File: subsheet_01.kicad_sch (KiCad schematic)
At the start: 0 parts

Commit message: Updated kicad-symbol-generated
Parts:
- added A1: FTDI_232H_MODULE_USB-C_VERSION_PHY, symbol 2264_bob_ft232h_usbc:FTDI_232H_MODULE_USB-C_VERSION_PHY
- added A2: FTDI_232H_MODULE_USB-A_VERSION_PHY, symbol bob_ft232h_usba:FTDI_232H_MODULE_USB-A_VERSION_PHY
- added J1: JTAG, symbol Connector_Generic:Conn_02x04_Odd_Even
- added J2: VPP connector, symbol Connector_Generic:Conn_02x01
- added J3: DC-DC converter, symbol Connector_Generic:Conn_01x04
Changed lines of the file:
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@@
     (company "Sporniket.com")
   )
+  (symbol (lib_id "Connector_Generic:Conn_01x04") (at 138.43 149.86 0) (unit 1)
+    (in_bom yes) (on_board yes) (dnp no)
+    (property "Reference" "J3" (at 138.43 144.78 0)
+      (effects (font (size 1.27 1.27)))
+    )
+    (property "Value" "DC-DC converter" (at 138.43 157.48 0)
+      (effects (font (size 1.27 1.27)))
+    )
+    (property "Footprint" "" (at 138.43 149.86 0)
+      (effects (font (size 1.27 1.27)) hide)
+    )
+    (property "Datasheet" "~" (at 138.43 149.86 0)
+      (effects (font (size 1.27 1.27)) hide)
+    )
+    (pin "4")
+    (pin "3")
+    (pin "2")
+    (pin "1")
+    (instances
+      (project "thomson-mo5--gate-array-development-board"
+        (path "/ba04bd6b-eda4-4852-8472-8c9205b270a0/aa83933c-d278-4584-ab2e-5bb5678ba36b"
+          (reference "J3") (unit 1)
+        )
+      )
+    )
+  )
+  (symbol (lib_id "bob_ft232h_usba:FTDI_232H_MODULE_USB-A_VERSION_PHY") (at 101.6 74.93 0) (unit 1)
+    (in_bom yes) (on_board yes) (dnp no)
+    (property "Reference" "A2" (at 93.98 55.88 0)
+      (effects (font (size 1.27 1.27)) (justify left top))
+    )
+    (property "Value" "FTDI_232H_MODULE_USB-A_VERSION_PHY" (at 93.98 58.42 0)
+      (effects (font (size 1.27 1.27) bold) (justify left top))
+    )
+    (property "Footprint" "" (at 101.6 74.93 0)
+      (effects (font (size 1.27 1.27)) hide)
+    )
+    (property "Datasheet" "_None_" (at 93.98 50.8 0)
+      (effects (font (size 1.27 1.27)) (justify left top) hide)
+    )
+    (pin "3")
+    (pin "2")
+    (pin "20")
+    (pin "19")
+    (pin "16")
+    (pin "13")
+    (pin "11")
+    (pin "7")
+    (pin "17")
+    (pin "1")
+    (pin "15")
+    (pin "5")
+    (pin "9")
+    (pin "4")
+    (pin "6")
+    (pin "8")
+    (pin "10")
+    (pin "14")
+    (pin "12")
+    (pin "18")
+    (instances
+      (project "thomson-mo5--gate-array-development-board"
+        (path "/ba04bd6b-eda4-4852-8472-8c9205b270a0/aa83933c-d278-4584-ab2e-5bb5678ba36b"
+          (reference "A2") (unit 1)
+        )
+      )
+    )
+  )
+  (symbol (lib_id "Connector_Generic:Conn_02x04_Odd_Even") (at 99.06 124.46 0) (unit 1)
+    (in_bom yes) (on_board yes) (dnp no)
+    (property "Reference" "J1" (at 100.33 119.38 0)
+      (effects (font (size 1.27 1.27)))
+    )
+    (property "Value" "JTAG" (at 100.33 132.08 0)
+      (effects (font (size 1.27 1.27)))
+    )
+    (property "Footprint" "" (at 99.06 124.46 0)
+      (effects (font (size 1.27 1.27)) hide)
+    )
+    (property "Datasheet" "~" (at 99.06 124.46 0)
+      (effects (font (size 1.27 1.27)) hide)
+    )
+    (pin "1")
+    (pin "4")
+    (pin "3")
+    (pin "2")
+    (pin "6")
+    (pin "7")
+    (pin "5")
+    (pin "8")
+    (instances
+      (project "thomson-mo5--gate-array-development-board"
+        (path "/ba04bd6b-eda4-4852-8472-8c9205b270a0/aa83933c-d278-4584-ab2e-5bb5678ba36b"
+          (reference "J1") (unit 1)
+        )
+      )
+    )
+  )
+  (symbol (lib_id "Connector_Generic:Conn_02x01") (at 99.06 147.32 0) (unit 1)
+    (in_bom yes) (on_board yes) (dnp no)
+    (property "Reference" "J2" (at 100.33 144.78 0)
+      (effects (font (size 1.27 1.27)))
+    )
+    (property "Value" "VPP connector" (at 100.33 149.86 0)
+      (effects (font (size 1.27 1.27)))
+    )
+    (property "Footprint" "" (at 99.06 147.32 0)
+      (effects (font (size 1.27 1.27)) hide)
+    )
+    (property "Datasheet" "~" (at 99.06 147.32 0)
+      (effects (font (size 1.27 1.27)) hide)
+    )
+    (pin "2")
+    (pin "1")
+    (instances
+      (project "thomson-mo5--gate-array-development-board"
+        (path "/ba04bd6b-eda4-4852-8472-8c9205b270a0/aa83933c-d278-4584-ab2e-5bb5678ba36b"
+          (reference "J2") (unit 1)
+        )
+      )
+    )
+  )
+  (symbol (lib_id "2264_bob_ft232h_usbc:FTDI_232H_MODULE_USB-C_VERSION_PHY") (at 101.6 38.1 0) (unit 1)
+    (in_bom yes) (on_board yes) (dnp no)
+    (property "Reference" "A1" (at 92.71 17.78 0)
+      (effects (font (size 1.27 1.27)) (justify left top))
+    )
+    (property "Value" "FTDI_232H_MODULE_USB-C_VERSION_PHY" (at 92.71 20.32 0)
+      (effects (font (size 1.27 1.27) bold) (justify left top))
+    )
+    (property "Footprint" "" (at 101.6 38.1 0)
+      (effects (font (size 1.27 1.27)) hide)
+    )
+    (property "Datasheet" "https://learn.adafruit.com/adafruit-ft232h-breakout/wiring" (at 92.71 12.7 0)
+      (effects (font (size 1.27 1.27)) (justify left top) hide)
+    )
+    (pin "9")
+    (pin "6")
+    (pin "14")
+    (pin "5")
+    (pin "20")
+    (pin "2")
+    (pin "18")
+    (pin "12")
+    (pin "11")
+    (pin "10")
+    (pin "1")
+    (pin "4")
+    (pin "22")
+    (pin "16")
+    (pin "21")
+    (pin "3")
+    (pin "7")
+    (pin "15")
+    (pin "17")
+    (pin "8")
+    (pin "13")
+    (pin "19")
+    (instances
+      (project "thomson-mo5--gate-array-development-board"
+        (path "/ba04bd6b-eda4-4852-8472-8c9205b270a0/aa83933c-d278-4584-ab2e-5bb5678ba36b"
+          (reference "A1") (unit 1)
+        )
+      )
+    )
+  )
 )

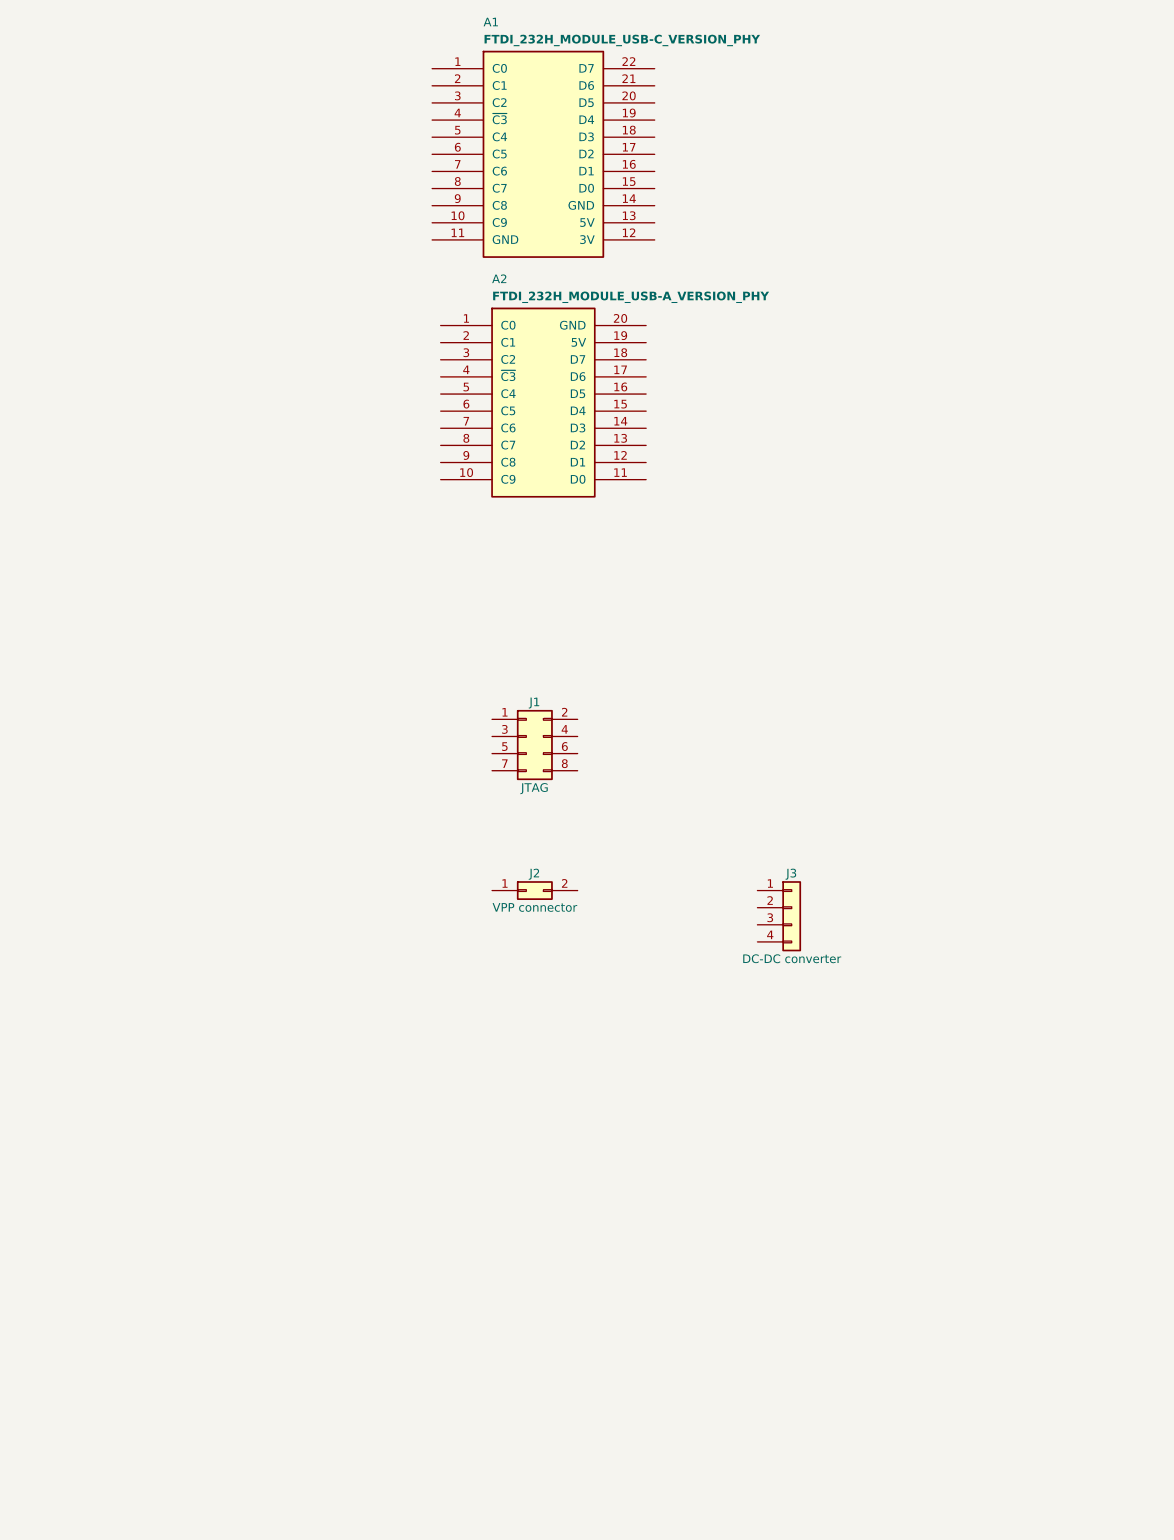
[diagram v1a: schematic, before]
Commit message: done schematics : ftdi module, JTAG, DC converters modules
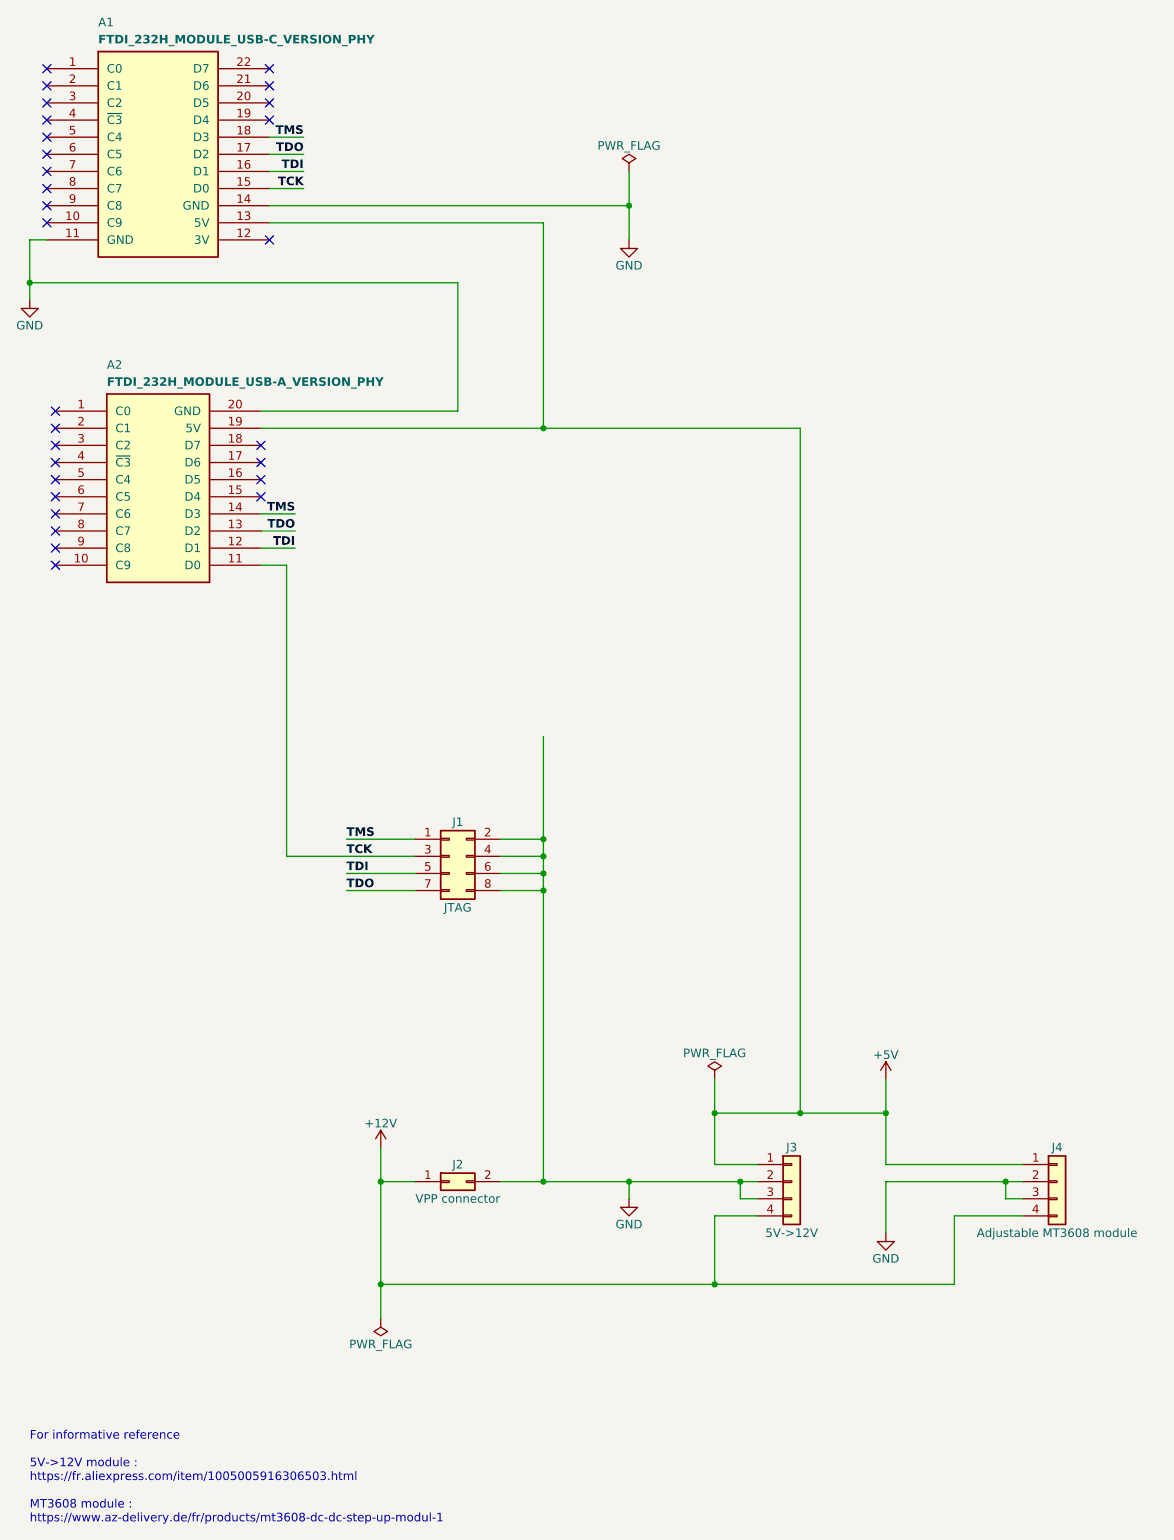
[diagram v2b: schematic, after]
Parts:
- added J4: Adjustable MT3608 module, symbol Connector_Generic:Conn_01x04
- J3: value DC-DC converter -> 5V->12V
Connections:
- net +5V: now reaches J3.1 (Pin_1)
- net +5V: now also A1.13 (5V), A2.19 (5V), J4.1 (Pin_1)
- net GND: now reaches J3.2 (Pin_2)
- net GND: now also A1.11 (GND), A1.14 (GND), A2.20 (GND), J1.2 (Pin_2), J1.4 (Pin_4), J1.6 (Pin_6), J1.8 (Pin_8), J2.2 (Pin_2), J3.3 (Pin_3), J4.2 (Pin_2), J4.3 (Pin_3)
- net +12V: now reaches J3.4 (Pin_4)
- net +12V: now also J2.1 (Pin_1), J4.4 (Pin_4)
- net TCK: now reaches A2.11 (D0)
- net TCK: now also A1.15 (D0), J1.3 (Pin_3)
- net TDI: now reaches A2.12 (D1)
- net TDI: now also A1.16 (D1), J1.5 (Pin_5)
- net TDO: now reaches A2.13 (D2)
- net TDO: now also A1.17 (D2), J1.7 (Pin_7)
- net TMS: now reaches A2.14 (D3)
- net TMS: now also A1.18 (D3), J1.1 (Pin_1)
- no-connect marks 0 -> 29
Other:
- note added: "For informative reference 5V->12V module : https://fr.aliexpress.com/item/1005005916306503.html MT3608 module : https://www.az-delivery.de/fr/products/mt3608-dc-dc-step-up-modul-1"
- moved on the sheet: A1, A2, J1, J2, J3

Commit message: done schematics
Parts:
- added D1, D2: LED, symbol Device:LED
- added R1, R2: 3K, symbol Device:R_Small_US
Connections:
- net +12V: now also D2.2 (A)
- net +5V: now also D1.2 (A)
- net GND: now also R1.2, R2.2
- new net: D1.1 (K), R1.1
- new net: D2.1 (K), R2.1

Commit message: assigned footprints, except for ftdi232h breakout boards
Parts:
- D1, D2: footprint (none) -> LED_THT:LED_D3.0mm
- J1: footprint (none) -> Connector_PinHeader_2.54mm:PinHeader_2x04_P2.54mm_Vertical
- J2: footprint (none) -> Connector_PinHeader_2.54mm:PinHeader_2x01_P2.54mm_Vertical
- J3: footprint (none) -> assemblies_power_modules:module_dc_dc_step_up_12V_W10.16mm_H20.5mm_PinSocket_1x04_P2.54mm_Horizontal
- J4: footprint (none) -> assemblies_power_modules:module_mt3608_ajustable_output
- R1, R2: footprint (none) -> commons-passives_THT:Passive_THT_resistor_W2.54mm_L12.70mm
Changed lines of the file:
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@@
       (effects (font (size 1.27 1.27)))
     )
-    (property "Footprint" "" (at 138.43 190.5 0)
+    (property "Footprint" "assemblies_power_modules:module_dc_dc_step_up_12V_W10.16mm_H20.5mm_PinSocket_1x04_P2.54mm_Horizontal" (at 138.43 190.5 0)
       (effects (font (size 1.27 1.27)) hide)
     )
@@
       (effects (font (size 1.27 1.27)) (justify left))
     )
-    (property "Footprint" "" (at 157.48 83.82 0)
+    (property "Footprint" "commons-passives_THT:Passive_THT_resistor_W2.54mm_L12.70mm" (at 157.48 83.82 0)
       (effects (font (size 1.27 1.27)) hide)
     )
@@
       (effects (font (size 1.27 1.27)) (justify left))
     )
-    (property "Footprint" "" (at 161.29 220.98 0)
+    (property "Footprint" "commons-passives_THT:Passive_THT_resistor_W2.54mm_L12.70mm" (at 161.29 220.98 0)
       (effects (font (size 1.27 1.27)) hide)
     )
@@
       (effects (font (size 1.27 1.27)))
     )
-    (property "Footprint" "" (at 152.4 215.9 0)
+    (property "Footprint" "LED_THT:LED_D3.0mm" (at 152.4 215.9 0)
       (effects (font (size 1.27 1.27)) hide)
     )
@@
       (effects (font (size 1.27 1.27)))
     )
-    (property "Footprint" "" (at 148.59 78.74 0)
+    (property "Footprint" "LED_THT:LED_D3.0mm" (at 148.59 78.74 0)
       (effects (font (size 1.27 1.27)) hide)
     )
@@
       (effects (font (size 1.27 1.27)))
     )
-    (property "Footprint" "" (at 87.63 142.24 0)
+    (property "Footprint" "Connector_PinHeader_2.54mm:PinHeader_2x04_P2.54mm_Vertical" (at 87.63 142.24 0)
       (effects (font (size 1.27 1.27)) hide)
     )
@@
       (effects (font (size 1.27 1.27)))
     )
-    (property "Footprint" "" (at 87.63 190.5 0)
+    (property "Footprint" "Connector_PinHeader_2.54mm:PinHeader_2x01_P2.54mm_Vertical" (at 87.63 190.5 0)
       (effects (font (size 1.27 1.27)) hide)
     )
@@
       (effects (font (size 1.27 1.27)))
     )
-    (property "Footprint" "" (at 177.8 190.5 0)
-      (effects (font (size 1.27 1.27)) hide)
-    )
+    (property "Footprint" "assemblies_power_modules:module_mt3608_ajustable_output" (at 177.8 190.5 0)
+      (effects (font (size 1.27 1.27)) hide)
+    )

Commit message: done pcb, missing labels and licence logo
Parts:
- A1: footprint (none) -> assemblies_ftdi232h:Adafruit_FT232H_breakout_USB_C
- A2: footprint (none) -> assemblies_ftdi232h:Noname_FT232H_breakout_USB_A
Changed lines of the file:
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@@
   (title_block
     (title "Thomson MO5 — Gate array development board")
-    (date "2025-07-08")
+    (date "2025-07-12")
     (rev "v0.0.0-draft")
     (company "Sporniket.com")
@@
       (effects (font (size 1.27 1.27) bold) (justify left top))
     )
-    (property "Footprint" "" (at 44.45 87.63 0)
+    (property "Footprint" "assemblies_ftdi232h:Noname_FT232H_breakout_USB_A" (at 44.45 87.63 0)
       (effects (font (size 1.27 1.27)) hide)
     )
@@
       (effects (font (size 1.27 1.27) bold) (justify left top))
     )
-    (property "Footprint" "" (at 44.45 38.1 0)
-      (effects (font (size 1.27 1.27)) hide)
-    )
+    (property "Footprint" "assemblies_ftdi232h:Adafruit_FT232H_breakout_USB_C" (at 44.45 38.1 0)
+      (effects (font (size 1.27 1.27)) hide)
+    )
